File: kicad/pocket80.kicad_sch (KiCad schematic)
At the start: 4 parts

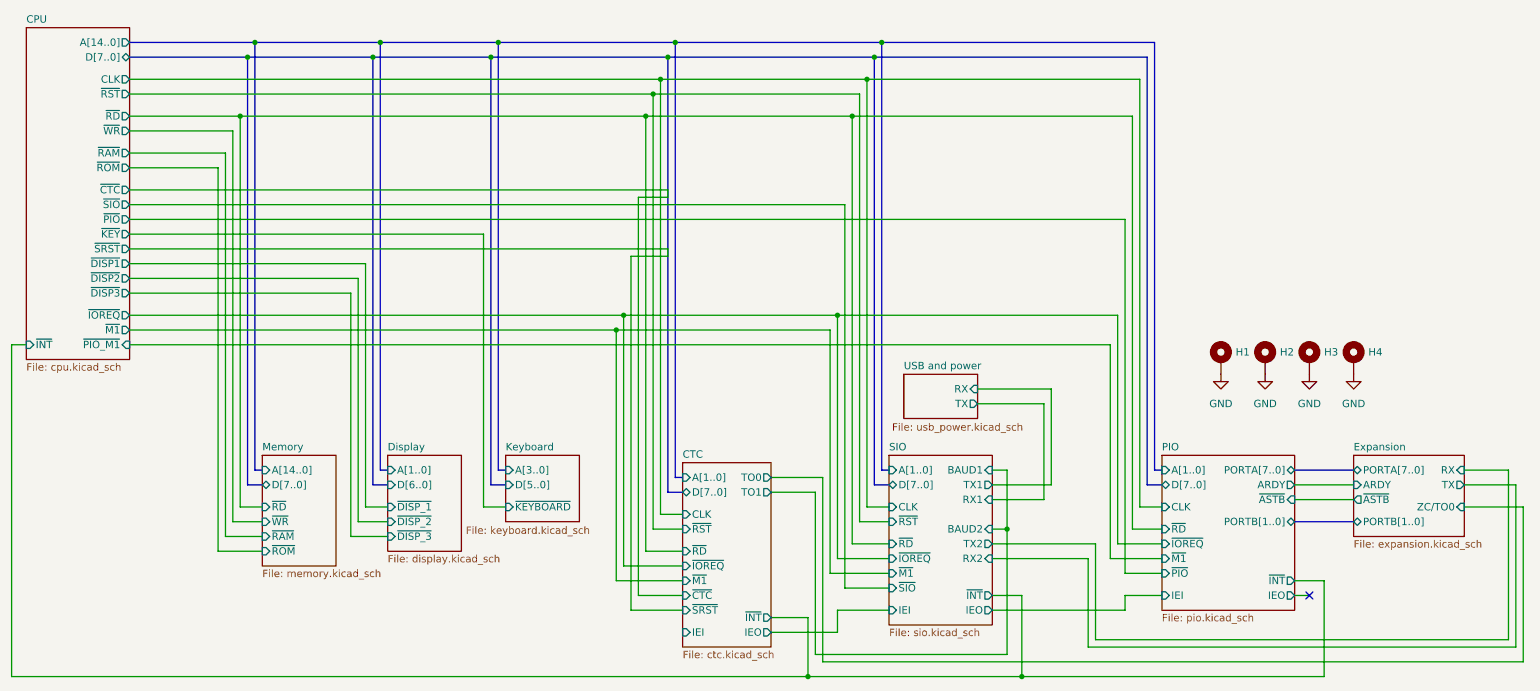
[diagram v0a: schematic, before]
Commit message: HW: Fix lack of /WR gating for DL1414
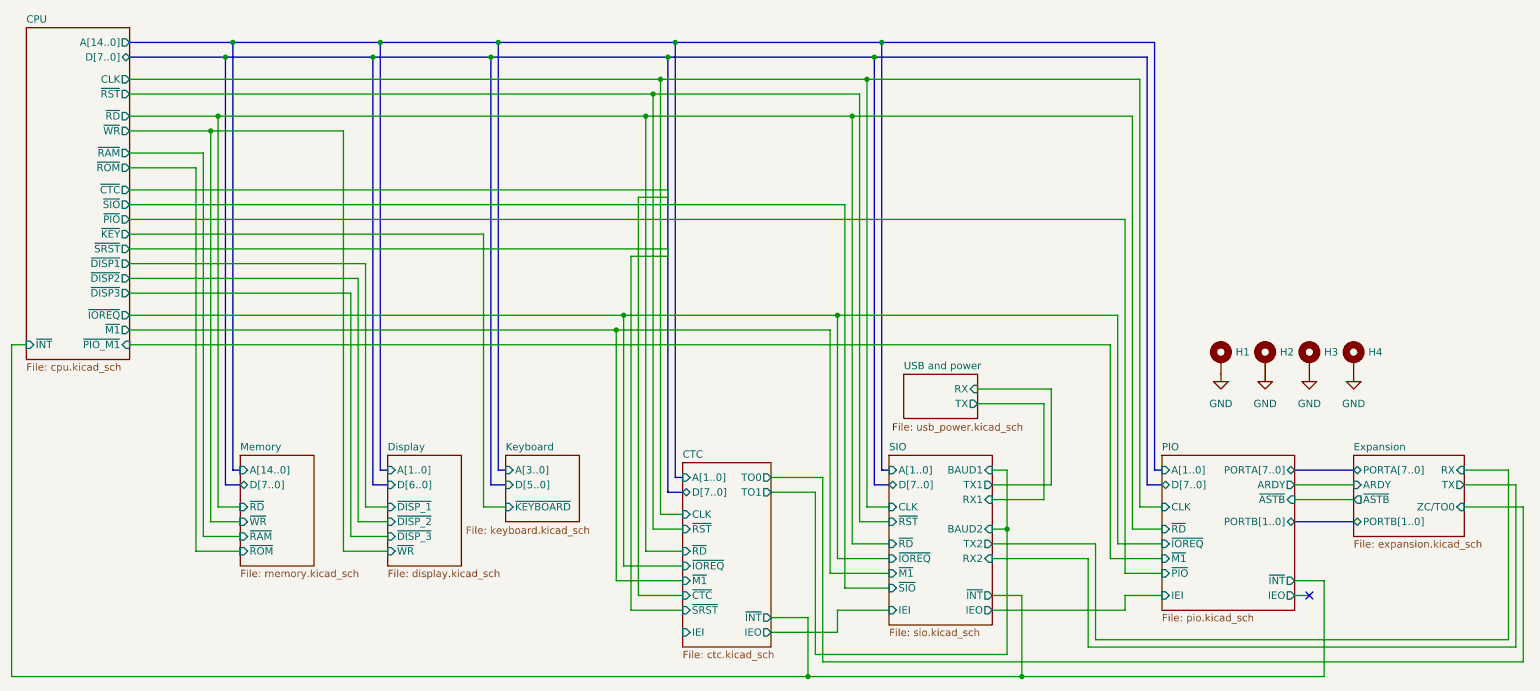
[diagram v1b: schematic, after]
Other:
- sheet Display ports: added ~{WR}; removed none
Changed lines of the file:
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@@
 	(paper "A4")
 	(title_block
-		(date "2025-10-19")
-		(rev "A")
+		(date "2025-11-03")
+		(rev "B")
 		(company "A.K.")
 	)
@@
 	)
 	(junction
-		(at 60.96 29.21)
-		(diameter 0)
-		(color 0 0 0 0)
-	)
-	(junction
 		(at 129.54 39.37)
 		(diameter 0)
@@
 	)
 	(junction
+		(at 54.61 41.91)
+		(diameter 0)
+		(color 0 0 0 0)
+	)
+	(junction
 		(at 167.64 33.02)
 		(diameter 0)
@@
 	)
 	(junction
-		(at 62.23 26.67)
+		(at 55.88 39.37)
 		(diameter 0)
 		(color 0 0 0 0)
@@
 	)
 	(junction
-		(at 59.69 39.37)
+		(at 191.77 110.49)
 		(diameter 0)
 		(color 0 0 0 0)
 	)
 	(junction
-		(at 191.77 110.49)
+		(at 58.42 26.67)
 		(diameter 0)
 		(color 0 0 0 0)
@@
 	)
 	(junction
+		(at 57.15 29.21)
+		(diameter 0)
+		(color 0 0 0 0)
+	)
+	(junction
 		(at 104.14 26.67)
 		(diameter 0)
@@
 	(wire
 		(pts
-			(xy 57.15 45.72) (xy 40.64 45.72)
+			(xy 53.34 45.72) (xy 40.64 45.72)
 		)
 		(stroke
@@
 	(wire
 		(pts
-			(xy 40.64 48.26) (xy 55.88 48.26)
+			(xy 40.64 48.26) (xy 52.07 48.26)
 		)
 		(stroke
@@
 	(wire
 		(pts
-			(xy 63.5 111.76) (xy 57.15 111.76)
+			(xy 59.69 111.76) (xy 53.34 111.76)
+		)
+		(stroke
+			(width 0)
+			(type default)
+		)
+	)
+	(wire
+		(pts
+			(xy 55.88 39.37) (xy 40.64 39.37)
 		)
 		(stroke
@@
 	(wire
 		(pts
+			(xy 77.47 114.3) (xy 85.09 114.3)
+		)
+		(stroke
+			(width 0)
+			(type default)
+		)
+	)
+	(wire
+		(pts
 			(xy 81.28 64.77) (xy 81.28 106.68)
 		)
@@
 	(wire
 		(pts
-			(xy 129.54 39.37) (xy 59.69 39.37)
-		)
-		(stroke
-			(width 0)
-			(type default)
-		)
-	)
-	(wire
-		(pts
 			(xy 162.56 128.27) (xy 162.56 124.46)
 		)
@@
 	(wire
 		(pts
-			(xy 59.69 106.68) (xy 59.69 39.37)
+			(xy 55.88 106.68) (xy 55.88 39.37)
 		)
 		(stroke
@@
 	(wire
 		(pts
-			(xy 63.5 109.22) (xy 58.42 109.22)
+			(xy 59.69 109.22) (xy 54.61 109.22)
 		)
 		(stroke
@@
 	(bus
 		(pts
-			(xy 40.64 26.67) (xy 62.23 26.67)
+			(xy 40.64 26.67) (xy 58.42 26.67)
 		)
 		(stroke
@@
 	(bus
 		(pts
-			(xy 63.5 102.87) (xy 60.96 102.87)
+			(xy 59.69 102.87) (xy 57.15 102.87)
 		)
 		(stroke
@@
 	(bus
 		(pts
-			(xy 60.96 29.21) (xy 60.96 102.87)
+			(xy 57.15 29.21) (xy 57.15 102.87)
 		)
 		(stroke
@@
 	(bus
 		(pts
-			(xy 63.5 100.33) (xy 62.23 100.33)
+			(xy 59.69 100.33) (xy 58.42 100.33)
 		)
 		(stroke
@@
 	(wire
 		(pts
-			(xy 58.42 41.91) (xy 40.64 41.91)
+			(xy 54.61 41.91) (xy 40.64 41.91)
 		)
 		(stroke
@@
 	(wire
 		(pts
-			(xy 59.69 39.37) (xy 40.64 39.37)
+			(xy 55.88 39.37) (xy 129.54 39.37)
 		)
 		(stroke
@@
 	(bus
 		(pts
-			(xy 62.23 26.67) (xy 83.82 26.67)
-		)
-		(stroke
-			(width 0)
-			(type default)
-		)
-	)
-	(bus
-		(pts
 			(xy 82.55 29.21) (xy 82.55 102.87)
 		)
@@
 	(bus
 		(pts
-			(xy 62.23 26.67) (xy 62.23 100.33)
+			(xy 58.42 26.67) (xy 58.42 100.33)
 		)
 		(stroke
@@
 		)
 	)
+	(bus
+		(pts
+			(xy 57.15 29.21) (xy 82.55 29.21)
+		)
+		(stroke
+			(width 0)
+			(type default)
+		)
+	)
 	(wire
 		(pts
@@
 	(bus
 		(pts
-			(xy 40.64 29.21) (xy 60.96 29.21)
+			(xy 40.64 29.21) (xy 57.15 29.21)
 		)
 		(stroke
@@
 	(wire
 		(pts
-			(xy 63.5 106.68) (xy 59.69 106.68)
-		)
-		(stroke
-			(width 0)
-			(type default)
-		)
-	)
-	(wire
-		(pts
-			(xy 57.15 111.76) (xy 57.15 45.72)
+			(xy 59.69 106.68) (xy 55.88 106.68)
+		)
+		(stroke
+			(width 0)
+			(type default)
+		)
+	)
+	(wire
+		(pts
+			(xy 53.34 111.76) (xy 53.34 45.72)
 		)
 		(stroke
@@
 		)
 	)
+	(wire
+		(pts
+			(xy 77.47 41.91) (xy 77.47 114.3)
+		)
+		(stroke
+			(width 0)
+			(type default)
+		)
+	)
 	(bus
 		(pts
@@
 	(wire
 		(pts
-			(xy 58.42 109.22) (xy 58.42 41.91)
+			(xy 54.61 109.22) (xy 54.61 41.91)
 		)
 		(stroke
@@
 		)
 	)
+	(bus
+		(pts
+			(xy 58.42 26.67) (xy 83.82 26.67)
+		)
+		(stroke
+			(width 0)
+			(type default)
+		)
+	)
 	(wire
 		(pts
@@
 	(wire
 		(pts
-			(xy 55.88 114.3) (xy 63.5 114.3)
+			(xy 52.07 114.3) (xy 59.69 114.3)
 		)
 		(stroke
@@
 	(wire
 		(pts
-			(xy 55.88 48.26) (xy 55.88 114.3)
+			(xy 52.07 48.26) (xy 52.07 114.3)
 		)
 		(stroke
@@
 		)
 	)
-	(bus
-		(pts
-			(xy 60.96 29.21) (xy 82.55 29.21)
-		)
-		(stroke
-			(width 0)
-			(type default)
-		)
-	)
 	(wire
 		(pts
@@
 		(pts
 			(xy 165.1 39.37) (xy 213.36 39.37)
+		)
+		(stroke
+			(width 0)
+			(type default)
+		)
+	)
+	(wire
+		(pts
+			(xy 54.61 41.91) (xy 77.47 41.91)
 		)
 		(stroke
@@
 	)
 	(sheet
-		(at 63.5 97.79)
+		(at 59.69 97.79)
 		(size 12.7 19.05)
 		(exclude_from_sim no)
@@
 		)
 		(property "Sheetname" "Memory"
-			(at 63.5 97.0784 0)
+			(at 59.69 97.0784 0)
 			(effects
 				(font
@@
 		)
 		(property "Sheetfile" "memory.kicad_sch"
-			(at 63.5 117.4246 0)
+			(at 59.69 117.4246 0)
 			(effects
 				(font
@@
 		)
 		(pin "A[14..0]" input
-			(at 63.5 100.33 180)
+			(at 59.69 100.33 180)
 			(effects
 				(font
@@
 		)
 		(pin "D[7..0]" bidirectional
-			(at 63.5 102.87 180)
+			(at 59.69 102.87 180)
 			(effects
 				(font
@@
 		)
 		(pin "~{RAM}" input
-			(at 63.5 111.76 180)
+			(at 59.69 111.76 180)
 			(effects
 				(font
@@
 		)
 		(pin "~{RD}" input
-			(at 63.5 106.68 180)
+			(at 59.69 106.68 180)
 			(effects
 				(font
@@
 		)
 		(pin "~{ROM}" input
-			(at 63.5 114.3 180)
+			(at 59.69 114.3 180)
 			(effects
 				(font
@@
 		)
 		(pin "~{WR}" input
-			(at 63.5 109.22 180)
+			(at 59.69 109.22 180)
 			(effects
 				(font
@@
 	(sheet
 		(at 85.09 97.79)
-		(size 12.7 16.51)
+		(size 12.7 19.05)
 		(exclude_from_sim no)
 		(in_bom yes)
@@
 		)
 		(property "Sheetfile" "display.kicad_sch"
-			(at 85.09 114.8846 0)
+			(at 85.09 117.4246 0)
 			(effects
 				(font
@@
 			(effects
 				(font
+					(size 1.27 1.27)
+				)
+				(justify left)
+			)
+		)
+		(pin "~{WR}" input
+			(at 85.09 114.3 180)
+			(effects
+				(font

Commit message: HW: Fix power switch pinout
thx kicad for no coherent pin numeration convention
and random shuffle on footprint assigment...
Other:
- title: (none) -> Pocket80
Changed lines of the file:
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@@
 	(paper "A4")
 	(title_block
-		(date "2025-12-04")
-		(rev "B")
+		(title "Pocket80")
+		(date "2025-12-17")
+		(rev "C")
 		(company "A.K.")
 	)

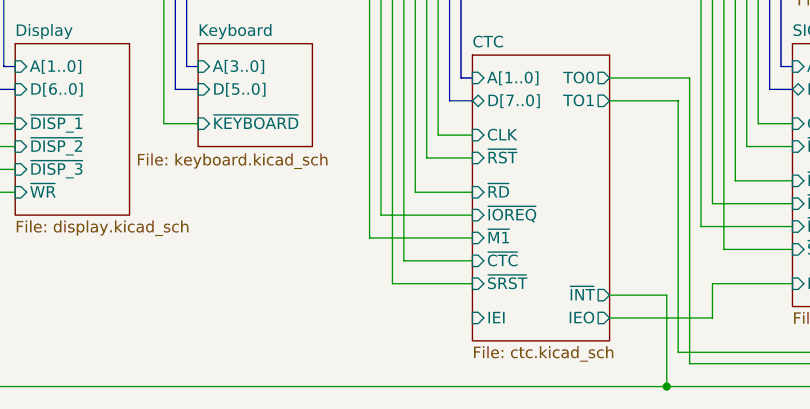
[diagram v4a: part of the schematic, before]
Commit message: HW: Fix initial IEI not being connected
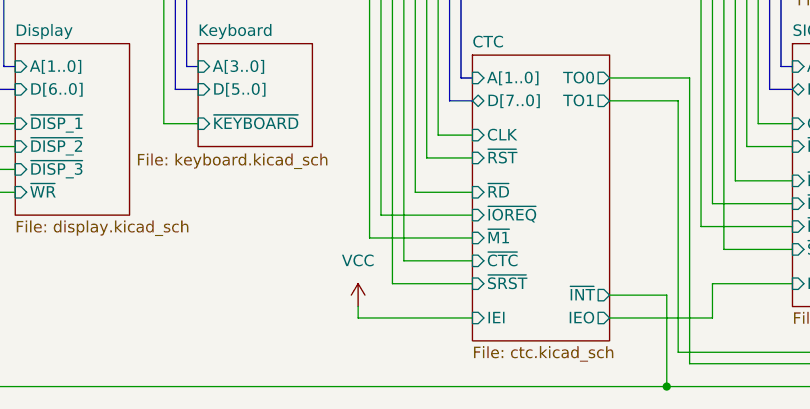
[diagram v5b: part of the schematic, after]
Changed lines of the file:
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@@
 	(title_block
 		(title "Pocket80")
-		(date "2025-12-17")
+		(date "2025-12-28")
 		(rev "C")
 		(company "A.K.")
@@
 	(wire
 		(pts
+			(xy 123.19 128.27) (xy 123.19 127)
+		)
+		(stroke
+			(width 0)
+			(type default)
+		)
+	)
+	(wire
+		(pts
 			(xy 278.13 129.54) (xy 278.13 100.33)
 		)
@@
 		(pts
 			(xy 83.82 26.67) (xy 104.14 26.67)
+		)
+		(stroke
+			(width 0)
+			(type default)
+		)
+	)
+	(wire
+		(pts
+			(xy 135.89 128.27) (xy 123.19 128.27)
 		)
 		(stroke
@@
 					(unit 1)
 				)
+			)
+		)
+	)
+	(symbol
+		(lib_id "power:VCC")
+		(at 123.19 127 0)
+		(unit 1)
+		(exclude_from_sim no)
+		(in_bom yes)
+		(on_board yes)
+		(dnp no)
+		(fields_autoplaced yes)
+		(property "Reference" "#PWR0154"
+			(at 123.19 130.81 0)
+			(effects
+				(font
+					(size 1.27 1.27)
+				)
+				(hide yes)
+			)
+		)
+		(property "Value" "VCC"
+			(at 123.19 121.92 0)
+			(effects
+				(font
+					(size 1.27 1.27)
+				)
+			)
+		)
+		(property "Footprint" ""
+			(at 123.19 127 0)
+			(effects
+				(font
+					(size 1.27 1.27)
+				)
+				(hide yes)
+			)
+		)
+		(property "Datasheet" ""
+			(at 123.19 127 0)
+			(effects
+				(font
+					(size 1.27 1.27)
+				)
+				(hide yes)
+			)
+		)
+		(property "Description" "Power symbol creates a global label with name \"VCC\""
+			(at 123.19 127 0)
+			(effects
+				(font
+					(size 1.27 1.27)
+				)
+				(hide yes)
+			)
+		)
+		(pin "1"
+		)
+		(instances
+			(project "pocket80"
+				(path "/328c075d-c706-4d2d-bd37-a88a0c604482"
+					(reference "#PWR0154")
+					(unit 1)
+				)
